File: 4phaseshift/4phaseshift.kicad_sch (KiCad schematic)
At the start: 25 parts, among them J1 Conn_Coaxial, J2 Conn_01x05_Pin, J3 Conn_Coaxial, J4 Conn_Coaxial, U1 AMS1117, U3 YSGM556006, U7 DAC43608

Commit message: gerbers generated for 4 element
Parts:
- added C6, C7: 10u, Capacitor_SMD:C_0603_1608Metric_Pad1.08x0.95mm_HandSolder, symbol Device:C_Small
- added C9: 1u, Capacitor_SMD:C_0603_1608Metric_Pad1.08x0.95mm_HandSolder, symbol Device:C_Small
- added R23: 300, Resistor_SMD:R_0603_1608Metric_Pad0.98x0.95mm_HandSolder, symbol Device:R_US
- added R24: 100, Resistor_SMD:R_0603_1608Metric_Pad0.98x0.95mm_HandSolder, symbol Device:R_US
- added U2: AMS1117, Package_TO_SOT_SMD:SOT-223-3_TabPin2, symbol Regulator_Linear:AMS1117
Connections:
- net GND: now also C6.1, C7.1, C9.1, R23.2
- net VCC: no longer RV1.3, U3.7 (VCC)
- net VS: now also C6.2, U2.3 (VI)
- net LDAC: now reaches J2.3 (Pin_3), U7.8 (LDAC)
- net SCL: now reaches J2.4 (Pin_4), U7.6 (SCL)
- net SDA: now reaches J2.5 (Pin_5), U7.5 (SDA)
- new net: R23.1, R24.2, U2.1 (ADJ)
- new net VCC2: C7.2, C9.2, R24.1, RV1.3, U2.2 (VO), U3.7 (VCC)
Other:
- sheet Amplifier_SBB5089Z1 ports: added LocalVCC; removed none
- sheet VectorModulator1 ports: added LocalVCC; removed none
- sheet VectorModulator2 ports: added LocalVCC; removed none
- sheet VectorModulator3 ports: added LocalVCC; removed none
- sheet VectorModulator4 ports: added LocalVCC; removed none

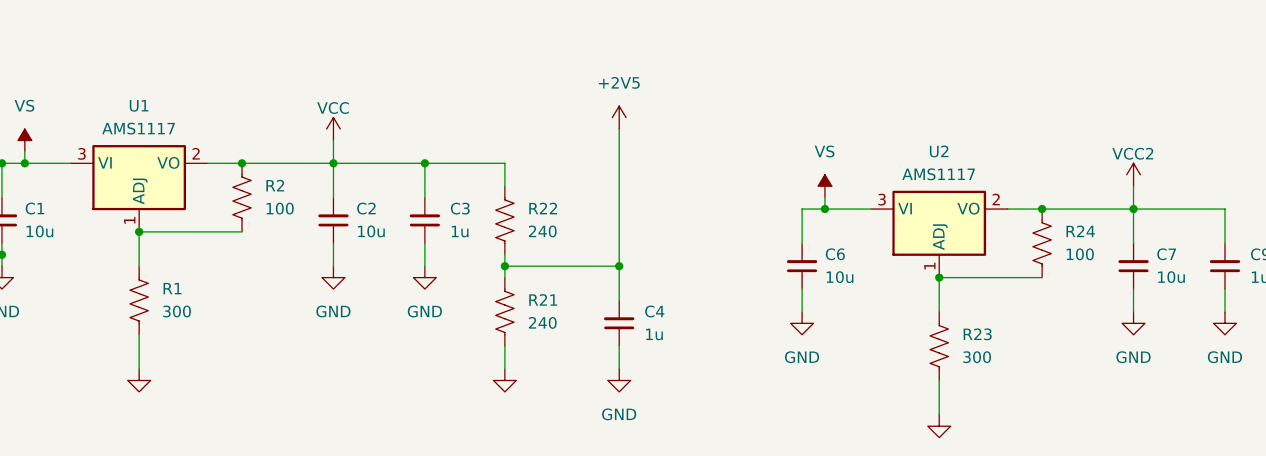
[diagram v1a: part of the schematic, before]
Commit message: updated resistor values
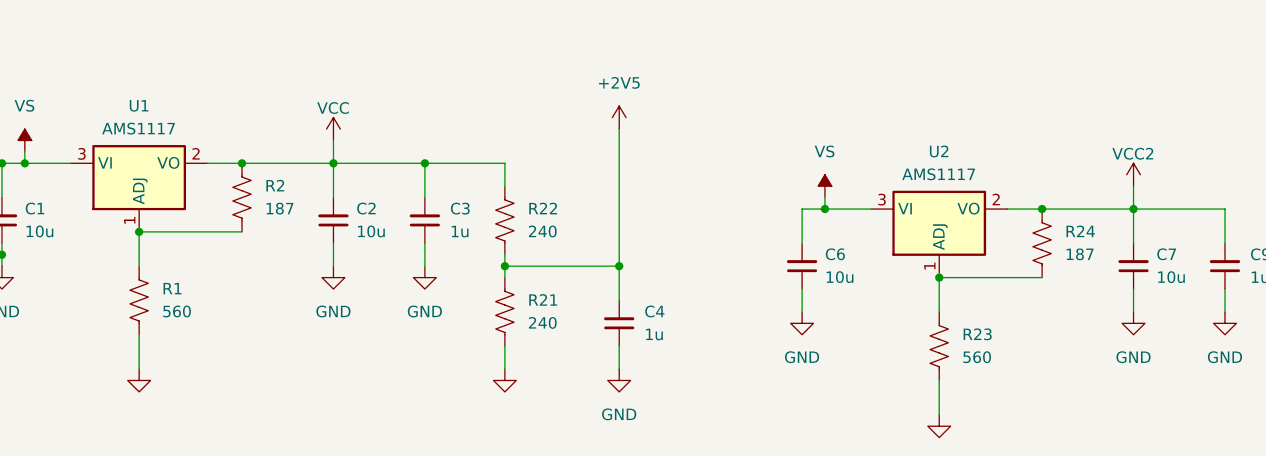
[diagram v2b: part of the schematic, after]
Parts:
- R1, R23: value 300 -> 560
- R2, R24: value 100 -> 187
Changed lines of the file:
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@@
 			)
 		)
-		(property "Value" "300"
+		(property "Value" "560"
 			(at 146.05 177.7999 0)
 			(effects
@@
 			)
 		)
-		(property "Value" "300"
+		(property "Value" "560"
 			(at 57.15 172.7199 0)
 			(effects
@@
 			)
 		)
-		(property "Value" "100"
+		(property "Value" "187"
 			(at 68.58 161.2899 0)
 			(effects
@@
 			)
 		)
-		(property "Value" "100"
+		(property "Value" "187"
 			(at 157.48 166.3699 0)
 			(effects
